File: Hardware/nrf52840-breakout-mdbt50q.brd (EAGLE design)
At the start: 47 x 22.9 mm, 110 parts, among them J8 CORTEX_DEBUG_PTH, U1 MDBT50Q, U2 MCP73831, U3 3.3V, Y1 32.768kHz

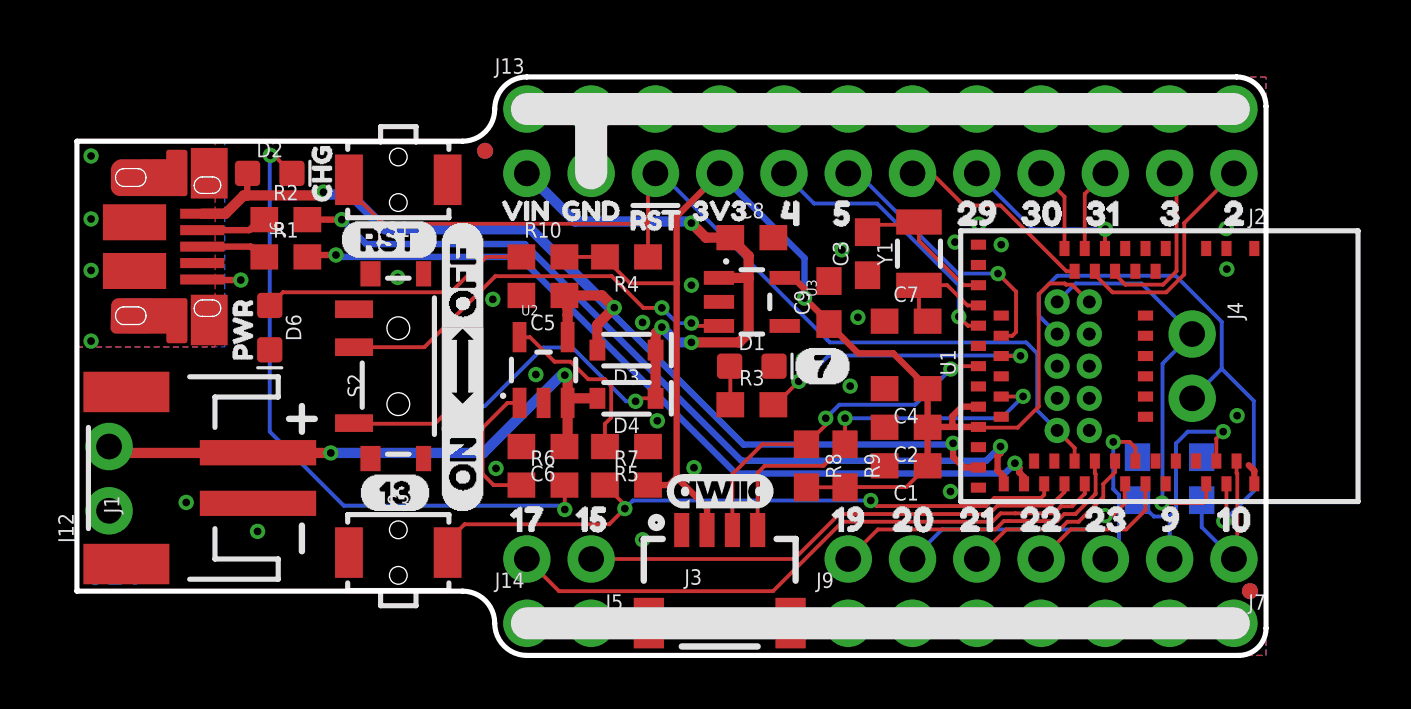
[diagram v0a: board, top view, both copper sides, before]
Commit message: Fixing silk on 28, 29, 30 bottom side
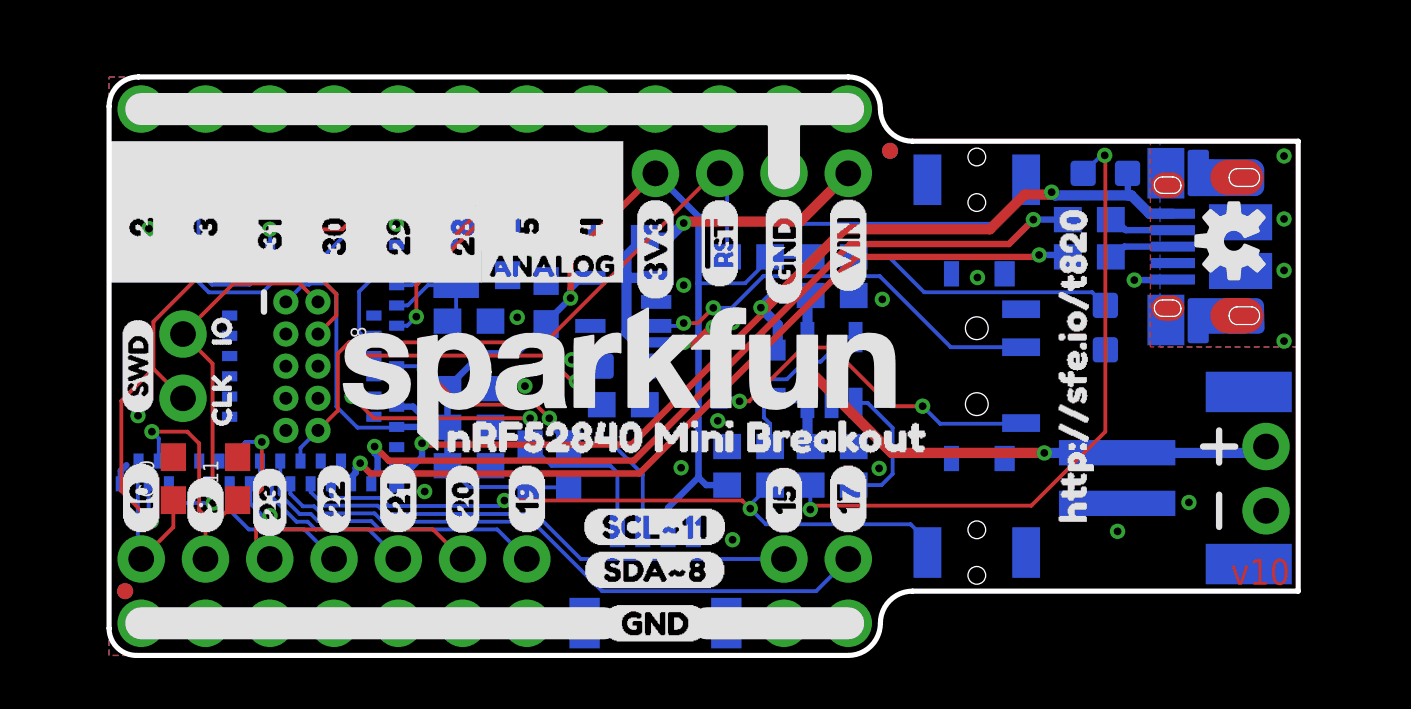
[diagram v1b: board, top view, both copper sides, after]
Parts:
- moved J12 45.7 mm to (47.0, 5.71), flipped to the bottom
- moved FD2 44.4 mm to (1.91, 2.54), flipped to the bottom
- moved FD3 44.4 mm to (1.91, 2.54), flipped to the top
- moved U$33 43.4 mm to (2.41, 9.53), flipped to the top
- moved FRAME1 43.2 mm to (45.7, -21.6), flipped to the bottom
- moved J2 43.2 mm to (2.54, 19.1), flipped to the bottom
- moved J7 43.2 mm to (2.54, 3.81), flipped to the bottom
- moved LOGO2 43.2 mm to (45.7, 16.4), flipped to the top
- moved U$21 43.2 mm to (2.54, 4.80), flipped to the top
- moved U$9 43.2 mm to (2.54, 15.7), flipped to the top
- moved J1 41.4 mm to (44.8, 7.01), flipped to the bottom
- moved C10 40.6 mm to (3.81, 6.99), flipped to the top
- moved U$31 40.4 mm to (3.94, 17.5), flipped to the bottom
- moved U$38 40.1 mm to (4.06, 5.38), flipped to the bottom
- moved J4 39.9 mm to (4.19, 12.7), flipped to the bottom
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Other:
- outline, holes or cut-outs redrawn

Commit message: Flipping board
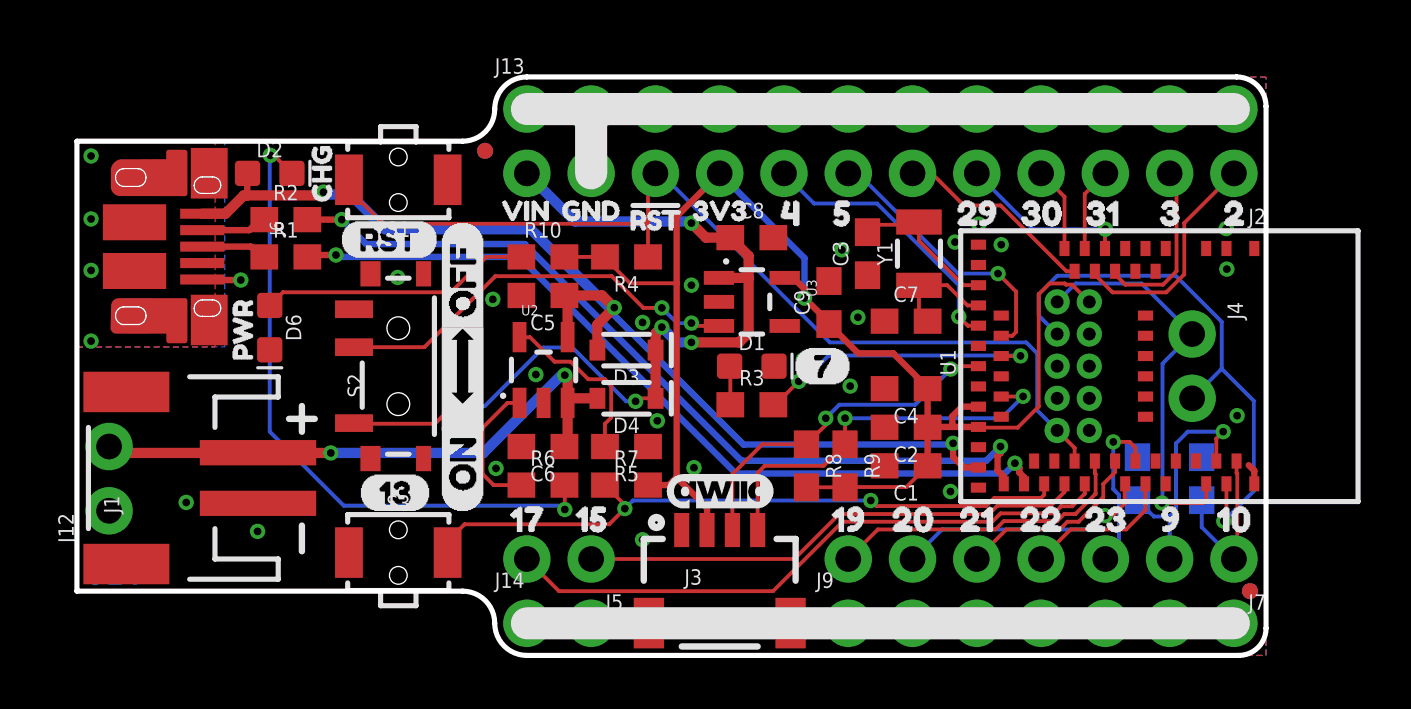
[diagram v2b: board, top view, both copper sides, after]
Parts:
- moved J12 45.7 mm to (1.27, 5.71), flipped to the top
- moved FD2 44.4 mm to (46.4, 2.54), flipped to the top
- moved FD3 44.4 mm to (46.4, 2.54), flipped to the bottom
- moved U$33 43.4 mm to (45.8, 9.53), flipped to the bottom
- moved FRAME1 43.2 mm to (2.54, -21.6), flipped to the top
- moved J2 43.2 mm to (45.7, 19.1), flipped to the top
- moved J7 43.2 mm to (45.7, 3.81), flipped to the top
- moved LOGO2 43.2 mm to (2.54, 16.4), flipped to the bottom
- moved U$21 43.2 mm to (45.7, 4.80), flipped to the bottom
- moved U$9 43.2 mm to (45.7, 15.7), flipped to the bottom
- moved J1 41.4 mm to (3.45, 7.01), flipped to the top
- moved C10 40.6 mm to (44.5, 6.99), flipped to the bottom
- moved U$31 40.4 mm to (44.3, 17.5), flipped to the top
- moved U$38 40.1 mm to (44.2, 5.38), flipped to the top
- moved J4 39.9 mm to (44.1, 12.7), flipped to the top
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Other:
- outline, holes or cut-outs redrawn
